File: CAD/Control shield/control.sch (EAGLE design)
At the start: 7 parts

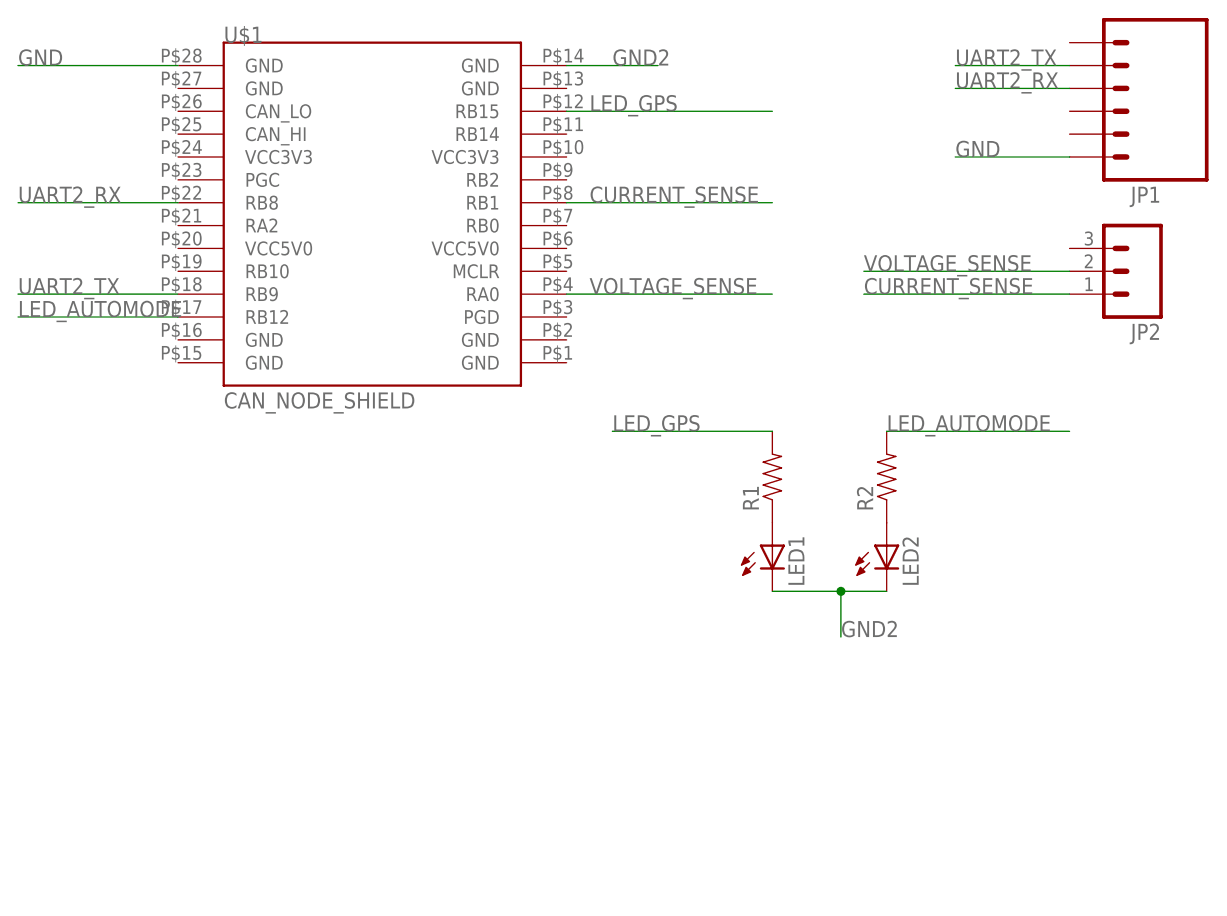
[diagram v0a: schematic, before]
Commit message: Added another 3-pin header for CAN to make debugging easier.
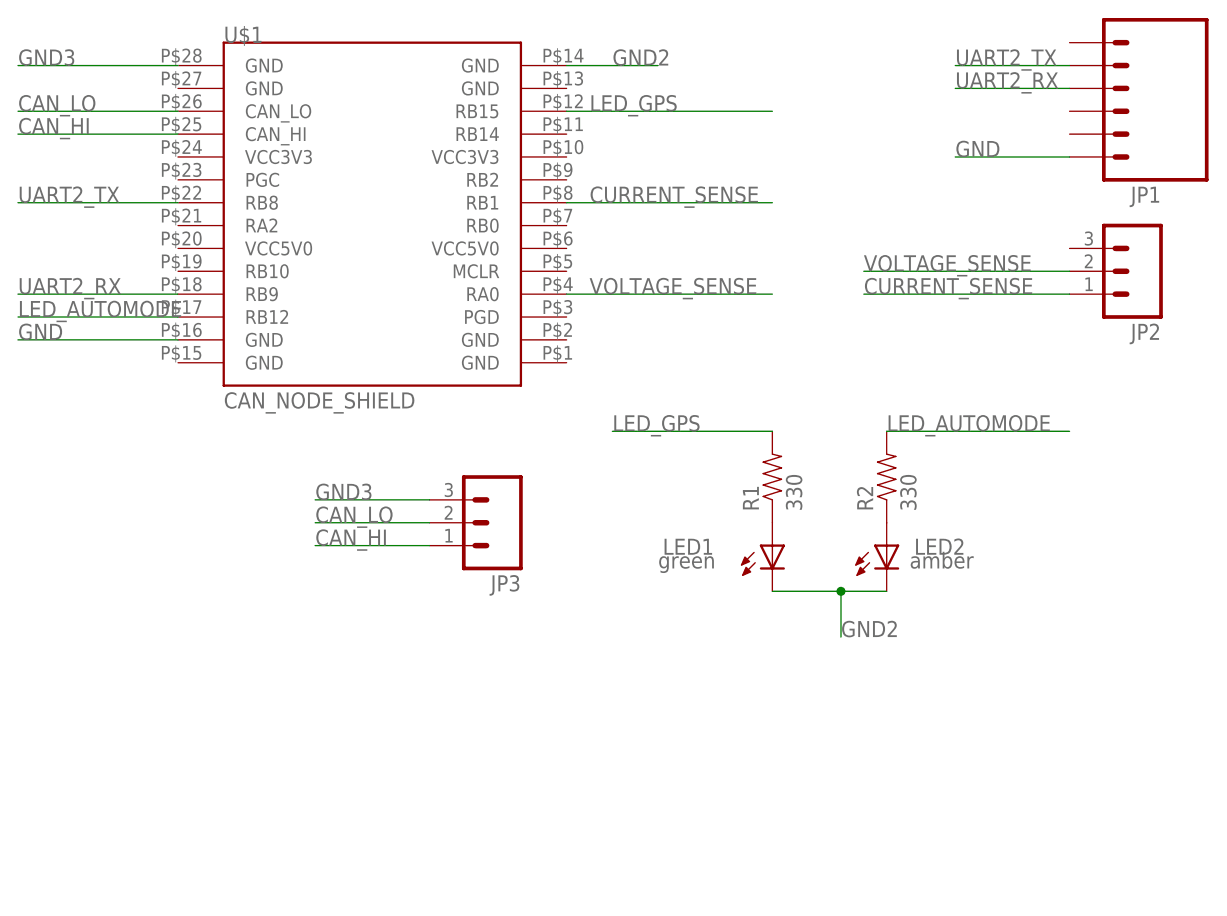
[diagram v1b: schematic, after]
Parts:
- added JP3: (no value), ASL:M03LOCK
- LED1: COLOR (none) -> green
- LED2: COLOR (none) -> amber
- R1, R2: value (none) -> 330
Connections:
- new net CAN_HI: JP3.1, U$1.CAN_HI
- new net CAN_LO: JP3.2, U$1.CAN_LO
- new net GND3: JP3.3, U$1.GND@28
- net GND: now also U$1.GND@16; no longer U$1.GND@28
- net UART2_RX: now also U$1.RB9; no longer U$1.RB8
- net UART2_TX: now also U$1.RB8; no longer U$1.RB9
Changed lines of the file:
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@@
 <part name="U$1" library="ASL" deviceset="CAN_NODE_SHIELD" device=""/>
 <part name="JP1" library="ASL" deviceset="M06" device="SIP_LOCK"/>
-<part name="LED1" library="ASL" deviceset="LED" device="1206"/>
-<part name="LED2" library="ASL" deviceset="LED" device="1206"/>
-<part name="R1" library="ASL" deviceset="RESISTOR" device="0805-RES"/>
-<part name="R2" library="ASL" deviceset="RESISTOR" device="0805-RES"/>
+<part name="LED1" library="ASL" deviceset="LED" device="1206">
+<attribute name="COLOR" value="green"/>
+</part>
+<part name="LED2" library="ASL" deviceset="LED" device="1206">
+<attribute name="COLOR" value="amber"/>
+</part>
+<part name="R1" library="ASL" deviceset="RESISTOR" device="0805-RES" value="330"/>
+<part name="R2" library="ASL" deviceset="RESISTOR" device="0805-RES" value="330"/>
 <part name="JP2" library="ASL" deviceset="M03" device="LOCK"/>
+<part name="JP3" library="ASL" deviceset="M03" device="LOCK"/>
 </parts>
 <sheets>
@@
 <instance part="U$1" gate="G$1" x="63.5" y="53.34"/>
 <instance part="JP1" gate="G$1" x="144.78" y="66.04" rot="R180"/>
-<instance part="LED1" gate="G$1" x="106.68" y="15.24"/>
-<instance part="LED2" gate="G$1" x="119.38" y="15.24"/>
+<instance part="LED1" gate="G$1" x="106.68" y="15.24" smashed="yes">
+<attribute name="COLOR" x="93.98" y="12.7" size="1.778" layer="96"/>
+<attribute name="NAME" x="94.488" y="14.224" size="1.778" layer="95"/>
+<attribute name="VALUE" x="112.395" y="10.668" size="1.778" layer="96" rot="R90"/>
+</instance>
+<instance part="LED2" gate="G$1" x="119.38" y="15.24" smashed="yes">
+<attribute name="COLOR" x="121.92" y="12.7" size="1.778" layer="96"/>
+<attribute name="NAME" x="122.428" y="14.224" size="1.778" layer="95"/>
+<attribute name="VALUE" x="125.095" y="10.668" size="1.778" layer="96" rot="R90"/>
+</instance>
 <instance part="R1" gate="G$1" x="106.68" y="22.86" rot="R90"/>
 <instance part="R2" gate="G$1" x="119.38" y="22.86" rot="R90"/>
 <instance part="JP2" gate="G$1" x="147.32" y="45.72" rot="R180"/>
+<instance part="JP3" gate="G$1" x="76.2" y="17.78" rot="R180"/>
 </instances>
 <busses>
@@
 <net name="UART2_RX" class="0">
 <segment>
-<pinref part="U$1" gate="G$1" pin="RB8"/>
-<wire x1="40.64" y1="53.34" x2="22.86" y2="53.34" width="0.1524" layer="91"/>
-<label x="22.86" y="53.34" size="1.778" layer="95"/>
-</segment>
-<segment>
 <pinref part="JP1" gate="G$1" pin="4"/>
 <wire x1="139.7" y1="66.04" x2="127" y2="66.04" width="0.1524" layer="91"/>
 <label x="127" y="66.04" size="1.778" layer="95"/>
 </segment>
-</net>
-<net name="UART2_TX" class="0">
 <segment>
 <pinref part="U$1" gate="G$1" pin="RB9"/>
@@
 <label x="22.86" y="43.18" size="1.778" layer="95"/>
 </segment>
+</net>
+<net name="UART2_TX" class="0">
 <segment>
 <pinref part="JP1" gate="G$1" pin="5"/>
 <wire x1="139.7" y1="68.58" x2="127" y2="68.58" width="0.1524" layer="91"/>
 <label x="127" y="68.58" size="1.778" layer="95"/>
+</segment>
+<segment>
+<pinref part="U$1" gate="G$1" pin="RB8"/>
+<wire x1="40.64" y1="53.34" x2="22.86" y2="53.34" width="0.1524" layer="91"/>
+<label x="22.86" y="53.34" size="1.778" layer="95"/>
 </segment>
 </net>
@@
 </segment>
 <segment>
-<pinref part="U$1" gate="G$1" pin="GND@28"/>
-<wire x1="40.64" y1="68.58" x2="22.86" y2="68.58" width="0.1524" layer="91"/>
-<label x="22.86" y="68.58" size="1.778" layer="95"/>
+<pinref part="U$1" gate="G$1" pin="GND@16"/>
+<wire x1="40.64" y1="38.1" x2="22.86" y2="38.1" width="0.1524" layer="91"/>
+<label x="22.86" y="38.1" size="1.778" layer="95"/>
 </segment>
 </net>
@@
 </segment>
 </net>
+<net name="GND3" class="0">
+<segment>
+<pinref part="JP3" gate="G$1" pin="3"/>
+<wire x1="68.58" y1="20.32" x2="55.88" y2="20.32" width="0.1524" layer="91"/>
+<label x="55.88" y="20.32" size="1.778" layer="95"/>
+</segment>
+<segment>
+<pinref part="U$1" gate="G$1" pin="GND@28"/>
+<wire x1="40.64" y1="68.58" x2="22.86" y2="68.58" width="0.1524" layer="91"/>
+<label x="22.86" y="68.58" size="1.778" layer="95"/>
+</segment>
+</net>
+<net name="CAN_LO" class="0">
+<segment>
+<pinref part="JP3" gate="G$1" pin="2"/>
+<wire x1="68.58" y1="17.78" x2="55.88" y2="17.78" width="0.1524" layer="91"/>
+<label x="55.88" y="17.78" size="1.778" layer="95"/>
+</segment>
+<segment>
+<pinref part="U$1" gate="G$1" pin="CAN_LO"/>
+<wire x1="40.64" y1="63.5" x2="22.86" y2="63.5" width="0.1524" layer="91"/>
+<label x="22.86" y="63.5" size="1.778" layer="95"/>
+</segment>
+</net>
+<net name="CAN_HI" class="2">
+<segment>
+<pinref part="JP3" gate="G$1" pin="1"/>
+<wire x1="55.88" y1="15.24" x2="68.58" y2="15.24" width="0.1524" layer="91"/>
+<label x="55.88" y="15.24" size="1.778" layer="95"/>
+</segment>
+<segment>
+<pinref part="U$1" gate="G$1" pin="CAN_HI"/>
+<wire x1="40.64" y1="60.96" x2="22.86" y2="60.96" width="0.1524" layer="91"/>
+<label x="22.86" y="60.96" size="1.778" layer="95"/>
+</segment>
+</net>

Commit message: Primary node shield:  * Removed defunct HIL/Revolution GS UART connection
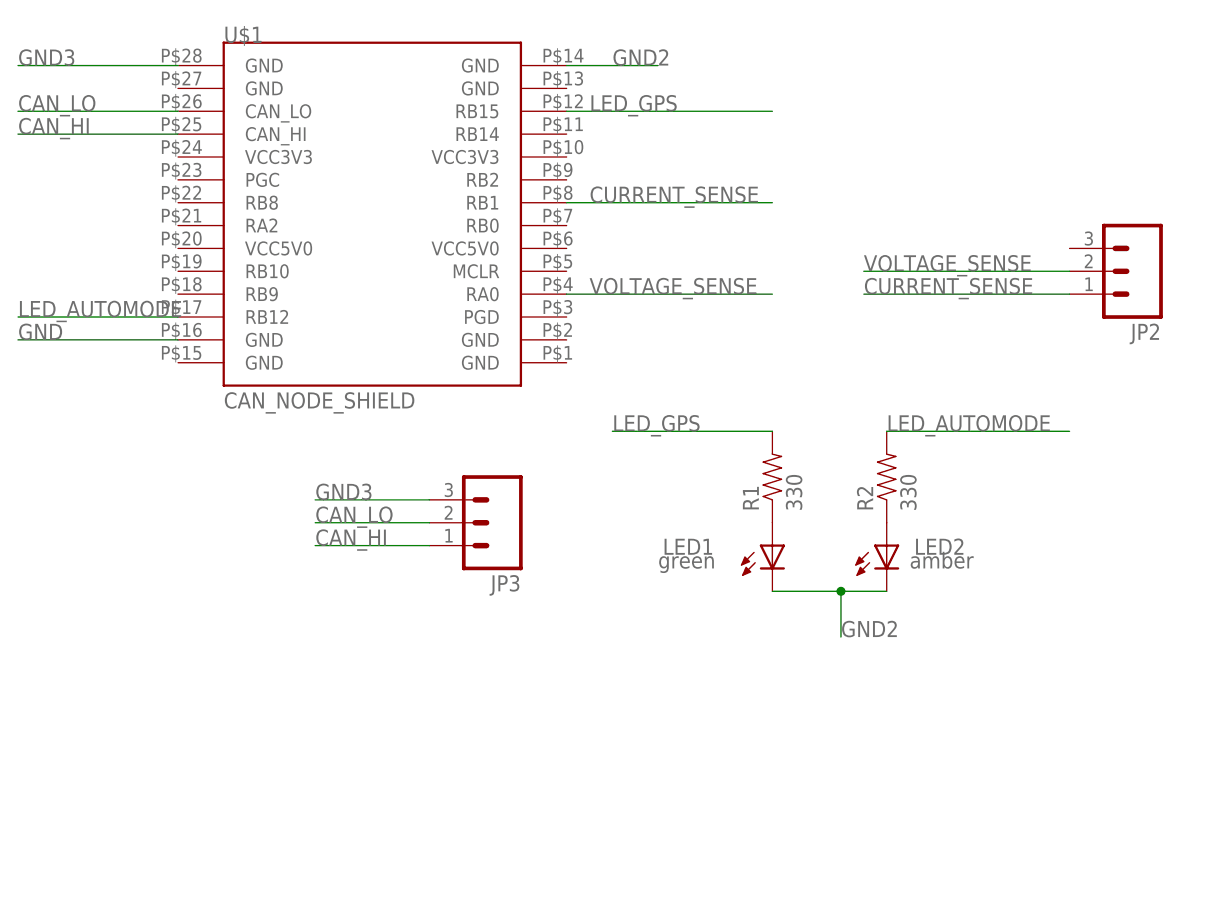
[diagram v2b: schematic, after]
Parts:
- removed JP1: (no value), ASL:M06SIP_LOCK
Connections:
- removed net UART2_RX: JP1.4, U$1.RB9
- removed net UART2_TX: JP1.5, U$1.RB8
- net GND: no longer JP1.1
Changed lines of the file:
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@@
 <parts>
 <part name="U$1" library="ASL" deviceset="CAN_NODE_SHIELD" device=""/>
-<part name="JP1" library="ASL" deviceset="M06" device="SIP_LOCK"/>
 <part name="LED1" library="ASL" deviceset="LED" device="1206">
 <attribute name="COLOR" value="green"/>
@@
 <instances>
 <instance part="U$1" gate="G$1" x="63.5" y="53.34"/>
-<instance part="JP1" gate="G$1" x="144.78" y="66.04" rot="R180"/>
 <instance part="LED1" gate="G$1" x="106.68" y="15.24" smashed="yes">
 <attribute name="COLOR" x="93.98" y="12.7" size="1.778" layer="96"/>
@@
 </segment>
 </net>
-<net name="UART2_RX" class="0">
-<segment>
-<pinref part="JP1" gate="G$1" pin="4"/>
-<wire x1="139.7" y1="66.04" x2="127" y2="66.04" width="0.1524" layer="91"/>
-<label x="127" y="66.04" size="1.778" layer="95"/>
-</segment>
-<segment>
-<pinref part="U$1" gate="G$1" pin="RB9"/>
-<wire x1="40.64" y1="43.18" x2="22.86" y2="43.18" width="0.1524" layer="91"/>
-<label x="22.86" y="43.18" size="1.778" layer="95"/>
-</segment>
-</net>
-<net name="UART2_TX" class="0">
-<segment>
-<pinref part="JP1" gate="G$1" pin="5"/>
-<wire x1="139.7" y1="68.58" x2="127" y2="68.58" width="0.1524" layer="91"/>
-<label x="127" y="68.58" size="1.778" layer="95"/>
-</segment>
-<segment>
-<pinref part="U$1" gate="G$1" pin="RB8"/>
-<wire x1="40.64" y1="53.34" x2="22.86" y2="53.34" width="0.1524" layer="91"/>
-<label x="22.86" y="53.34" size="1.778" layer="95"/>
-</segment>
-</net>
 <net name="GND" class="1">
 <segment>
-<pinref part="JP1" gate="G$1" pin="1"/>
-<wire x1="139.7" y1="58.42" x2="127" y2="58.42" width="0.1524" layer="91"/>
-<label x="127" y="58.42" size="1.778" layer="95"/>
-</segment>
-<segment>
 <pinref part="U$1" gate="G$1" pin="GND@16"/>

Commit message: Updated the control shield to the CANode v3 shield layout.
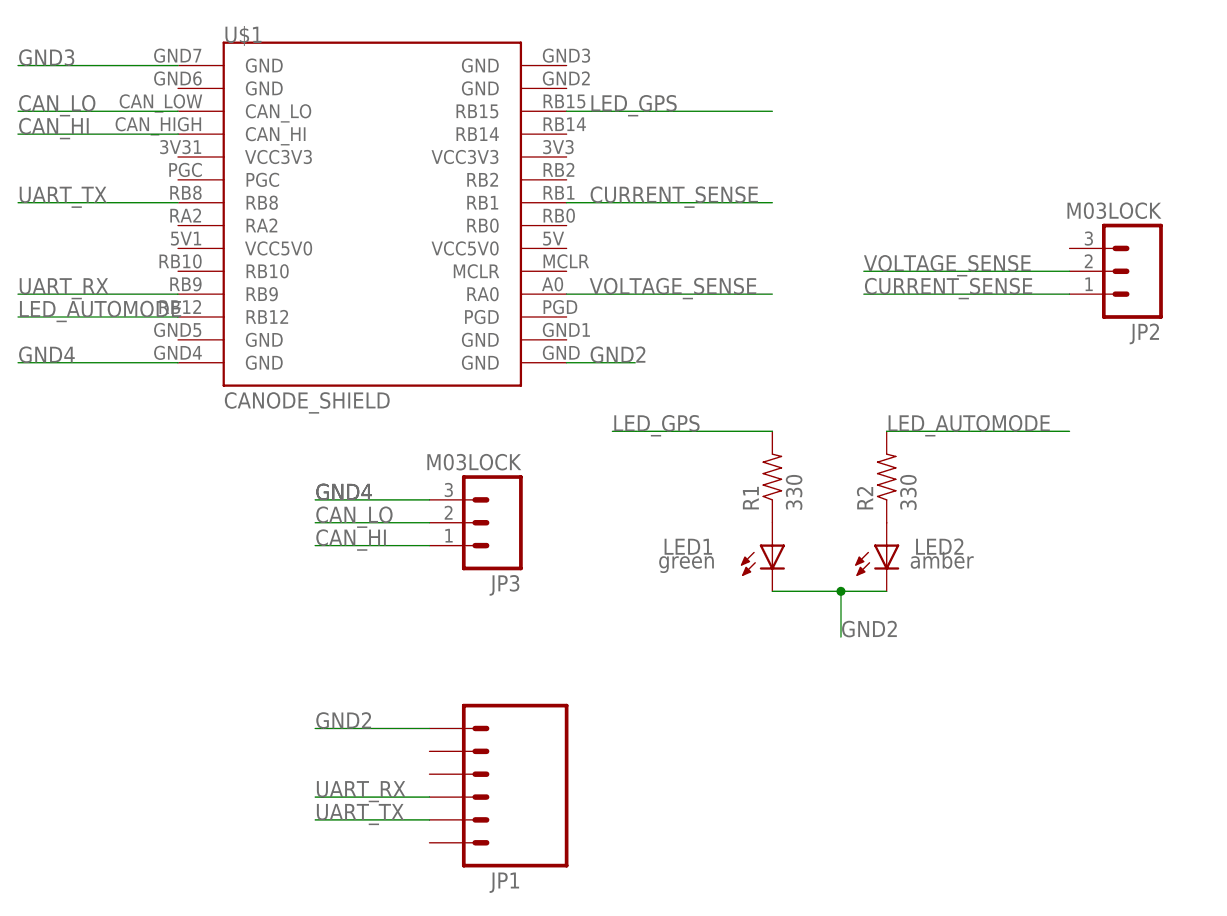
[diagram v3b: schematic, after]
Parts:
- added JP1: (no value), ASL:M06LOCK
- JP2, JP3: value (none) -> M03LOCK
- U$1: value CAN_NODE_SHIELD -> CANODE_SHIELD; device ASL:CAN_NODE_SHIELD -> ASL:CANODE_SHIELD
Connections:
- removed net GND: U$1.GND@16
- new net GND4: JP3.3, U$1.GND@15
- new net UART_RX: JP1.3, U$1.RB9
- new net UART_TX: JP1.2, U$1.RB8
- net GND2: now also JP1.6, U$1.GND@1; no longer U$1.GND@14
- net GND3: no longer JP3.3
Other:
- moved on the sheet: U$1
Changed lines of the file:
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@@
 </variantdefs>
 <classes>
-<class number="0" name="default" width="0.4572" drill="0">
+<class number="0" name="default" width="0.4064" drill="0">
 </class>
 <class number="1" name="power" width="0.762" drill="0">
 </class>
-<class number="2" name="small" width="0.254" drill="0">
+<class number="2" name="small" width="0.2032" drill="0">
 </class>
 </classes>
 <parts>
-<part name="U$1" library="ASL" deviceset="CAN_NODE_SHIELD" device=""/>
+<part name="U$1" library="ASL" deviceset="CANODE_SHIELD" device=""/>
 <part name="LED1" library="ASL" deviceset="LED" device="1206">
 <attribute name="COLOR" value="green"/>
@@
 <part name="JP2" library="ASL" deviceset="M03" device="LOCK"/>
 <part name="JP3" library="ASL" deviceset="M03" device="LOCK"/>
+<part name="JP1" library="ASL" deviceset="M06" device="LOCK"/>
 </parts>
 <sheets>
@@
 <instance part="JP2" gate="G$1" x="147.32" y="45.72" rot="R180"/>
 <instance part="JP3" gate="G$1" x="76.2" y="17.78" rot="R180"/>
+<instance part="JP1" gate="G$1" x="73.66" y="-10.16" rot="R180"/>
 </instances>
 <busses>
@@
 </segment>
 </net>
-<net name="GND" class="1">
-<segment>
-<pinref part="U$1" gate="G$1" pin="GND@16"/>
-<wire x1="40.64" y1="38.1" x2="22.86" y2="38.1" width="0.1524" layer="91"/>
-<label x="22.86" y="38.1" size="1.778" layer="95"/>
-</segment>
-</net>
-<net name="LED_AUTOMODE" class="0">
+<net name="LED_AUTOMODE" class="2">
 <segment>
 <pinref part="U$1" gate="G$1" pin="RB12"/>
@@
 <net name="GND2" class="0">
 <segment>
-<pinref part="U$1" gate="G$1" pin="GND@14"/>
-<wire x1="83.82" y1="68.58" x2="93.98" y2="68.58" width="0.1524" layer="91"/>
-<label x="88.9" y="68.58" size="1.778" layer="95"/>
-</segment>
-<segment>
 <pinref part="LED1" gate="G$1" pin="C"/>
 <pinref part="LED2" gate="G$1" pin="C"/>
@@
 <junction x="114.3" y="10.16"/>
 </segment>
+<segment>
+<pinref part="U$1" gate="G$1" pin="GND@1"/>
+<wire x1="83.82" y1="35.56" x2="91.44" y2="35.56" width="0.1524" layer="91"/>
+<label x="86.36" y="35.56" size="1.778" layer="95"/>
+</segment>
+<segment>
+<pinref part="JP1" gate="G$1" pin="6"/>
+<wire x1="68.58" y1="-5.08" x2="55.88" y2="-5.08" width="0.1524" layer="91"/>
+<label x="55.88" y="-5.08" size="1.778" layer="95"/>
+</segment>
 </net>
 <net name="GND3" class="0">
-<segment>
-<pinref part="JP3" gate="G$1" pin="3"/>
-<wire x1="68.58" y1="20.32" x2="55.88" y2="20.32" width="0.1524" layer="91"/>
-<label x="55.88" y="20.32" size="1.778" layer="95"/>
-</segment>
 <segment>
 <pinref part="U$1" gate="G$1" pin="GND@28"/>
@@
 </segment>
 </net>
+<net name="GND4" class="0">
+<segment>
+<pinref part="U$1" gate="G$1" pin="GND@15"/>
+<wire x1="40.64" y1="35.56" x2="22.86" y2="35.56" width="0.1524" layer="91"/>
+<label x="22.86" y="35.56" size="1.778" layer="95"/>
+</segment>
+<segment>
+<pinref part="JP3" gate="G$1" pin="3"/>
+<wire x1="68.58" y1="20.32" x2="55.88" y2="20.32" width="0.1524" layer="91"/>
+<label x="55.88" y="20.32" size="1.778" layer="95"/>
+<label x="55.88" y="20.32" size="1.778" layer="95"/>
+</segment>
+</net>
+<net name="UART_RX" class="0">
+<segment>
+<pinref part="JP1" gate="G$1" pin="3"/>
+<wire x1="68.58" y1="-12.7" x2="55.88" y2="-12.7" width="0.1524" layer="91"/>
+<label x="55.88" y="-12.7" size="1.778" layer="95"/>
+</segment>
+<segment>
+<pinref part="U$1" gate="G$1" pin="RB9"/>
+<wire x1="40.64" y1="43.18" x2="22.86" y2="43.18" width="0.1524" layer="91"/>
+<label x="22.86" y="43.18" size="1.778" layer="95"/>
+</segment>
+</net>
+<net name="UART_TX" class="0">
+<segment>
+<pinref part="JP1" gate="G$1" pin="2"/>
+<wire x1="68.58" y1="-15.24" x2="55.88" y2="-15.24" width="0.1524" layer="91"/>
+<label x="55.88" y="-15.24" size="1.778" layer="95"/>
+</segment>
+<segment>
+<pinref part="U$1" gate="G$1" pin="RB8"/>
+<wire x1="40.64" y1="53.34" x2="22.86" y2="53.34" width="0.1524" layer="91"/>
+<label x="22.86" y="53.34" size="1.778" layer="95"/>
+</segment>
+</net>
